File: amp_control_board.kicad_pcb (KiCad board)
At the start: 2 copper layers, 75 parts, among them J1 Conn_01x03_Male, J2 Conn_01x04_Female, J3 Screw_Terminal_01x03, J4 Screw_Terminal_01x02, J5 Conn_01x04_Female, J6 Conn_02x03_Odd_Even, J7 Conn_01x03_Male, M1 Fan_4pin, M2 Fan_4pin, Q1 BSP89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

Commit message: changing dev pc
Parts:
- moved SW3 78.4 mm to (113.4, 40.2)
- moved SW4 78.4 mm to (118.1, 40.2)
- moved U3 78.4 mm to (44.9, 74.5)
- moved C10 78.4 mm to (97.5, 77.7)
- moved C12 78.4 mm to (78.1, 82.5)
- moved C14 78.4 mm to (92.6, 71.8)
- moved C18 78.4 mm to (119.6, 55.4)
- moved C6 78.4 mm to (73.4, 82.5)
- moved C9 78.4 mm to (55.0, 80.1)
- moved D1 78.4 mm to (83.4, 64.9)
- moved D2 78.4 mm to (111.9, 52.4)
- moved J3 78.4 mm to (28.1, 66.0)
- moved J4 78.4 mm to (54.2, 74.0)
- moved J6 78.4 mm to (125.2, 35.7)
- moved J7 78.4 mm to (108.8, 58.1)
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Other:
- board outline added: 100.1 x 61 mm
- rule trace_min: 0.2 -> 0.1016
- rule via_min_drill: 0.3 -> 0.254
- rule via_min_size: 0.4 -> 0.254

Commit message: started floorplan
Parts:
- moved C9 146.2 mm to (173.0, -6.35), turned to 90 degrees
- moved DS1 146.1 mm to (282.6, 57.1)
- moved Y2 140.0 mm to (150.2, 158.7)
- moved D3 138.8 mm to (147.3, 182.2)
- moved C7 138.0 mm to (141.6, -20.3), turned to 90 degrees
- moved J1 136.3 mm to (172.7, 154.3), turned to 180 degrees
- moved J6 135.2 mm to (124.5, 170.8)
- moved U3 134.3 mm to (151.1, -7.62), turned to 270 degrees
- moved C5 134.0 mm to (134.6, -24.8), turned to 180 degrees
- moved R7 131.8 mm to (142.2, 182.2)
- moved R15 129.4 mm to (135.9, 173.4)
- moved C1 126.8 mm to (121.5, -24.8)
- moved Y1 125.7 mm to (146.1, 140.3)
- moved U1 125.6 mm to (151.8, -21.0)
- moved C8 125.6 mm to (157.5, 161.9)
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
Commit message: Adding changes 2008
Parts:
- J1, J3, M1, M2, SW2, SW3, SW4: moved to B.Cu
- moved M1 200.8 mm to (210.2, 74.3), turned to 180 degrees
- moved R23 188.7 mm to (214.6, 71.1)
- moved M2 185.9 mm to (175.3, 74.3), turned to 180 degrees
- moved SW4 185.9 mm to (215.3, 111.8)
- moved SW3 182.8 mm to (204.5, 111.8)
- moved SW2 179.3 mm to (193.7, 111.8)
- moved J3 173.3 mm to (133.3, 111.8), turned to 270 degrees
- moved R22 172.5 mm to (218.4, 71.1)
- moved R26 156.0 mm to (184.8, 71.8)
- moved R27 136.9 mm to (179.8, 71.8)
- moved R19 130.5 mm to (209.6, 110.5), turned to 90 degrees
- moved R18 128.6 mm to (209.6, 104.8), turned to 90 degrees
- moved R3 127.4 mm to (220.0, 75.6)
- moved R25 126.3 mm to (186.1, 76.2)
- moved R20 125.8 mm to (220.3, 104.8), turned to 90 degrees
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
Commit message: finished floorplan of top layer
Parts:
- C1: footprint Capacitor_SMD:C_0805_2012Metric_Pad1.18x1.45mm_HandSolder -> Capacitor_SMD:CP_Elec_10x12.5
- C13, C15, C16, C18: footprint Resistor_SMD:R_0805_2012Metric_Pad1.20x1.40mm_HandSolder -> Resistor_SMD:R_0402_1005Metric_Pad0.72x0.64mm_HandSolder
- C5, C7, C9: footprint Capacitor_SMD:C_0805_2012Metric_Pad1.18x1.45mm_HandSolder -> Capacitor_SMD:CP_Elec_10x10
- J3: value Screw_Terminal_01x03 -> Conn_01x03_Male; footprint TerminalBlock:TerminalBlock_bornier-3_P5.08mm -> Connector_PinHeader_2.54mm:PinHeader_1x03_P2.54mm_Vertical
- moved DS1 260.5 mm to (37.5, 145.4)
- moved C9 175.6 mm to (51.7, 120.7)
- moved U1 175.6 mm to (30.5, 106.0)
- moved U3 175.6 mm to (29.8, 119.4)
- moved C7 148.6 mm to (72.4, 111.1)
- moved C1 143.2 mm to (56.5, 102.9)
- moved U2 143.0 mm to (53.3, 90.8)
- moved C5 136.6 mm to (71.8, 96.5), turned to 270 degrees
- moved J4 135.1 mm to (28.6, 70.5)
- moved C11 101.2 mm to (185.4, 121.9)
- moved SW1 100.7 mm to (184.8, 116.8)
- moved R4 99.6 mm to (180.3, 121.9), turned to 180 degrees
- moved J7 97.8 mm to (28.6, 52.1)
- moved D3 89.2 mm to (140.3, 93.3)
- moved R7 89.1 mm to (135.9, 93.3)
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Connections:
- U5 pad 39: Net-(U5-Pad39) -> BTN_MODE
- U5 pad 40: Net-(U5-Pad40) -> BTN_UP
- U5 pad 41: Net-(U5-Pad41) -> BTN_DOWN

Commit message: completed preliminary floorplan for both top and bottom
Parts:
- C1, C5, C7, C9, J2, J4, J7, U1, U2, U3: moved to B.Cu
- moved U3 140.7 mm to (170.2, 108.6), turned to 0 degrees
- moved J2 132.4 mm to (155.6, 71.1), turned to 270 degrees
- moved U1 126.8 mm to (156.8, 95.2), turned to 180 degrees
- moved C9 122.9 mm to (172.1, 95.9)
- moved J7 115.9 mm to (132.7, 102.9)
- moved J4 105.4 mm to (134.0, 72.4)
- moved U2 92.8 mm to (146.1, 85.7), turned to 90 degrees
- moved C5 86.1 mm to (156.8, 83.2)
- moved C7 84.6 mm to (156.8, 106.7), turned to 180 degrees
- moved C1 82.4 mm to (136.5, 83.2), turned to 180 degrees
- moved DS1 12.1 mm to (29.2, 154.3)

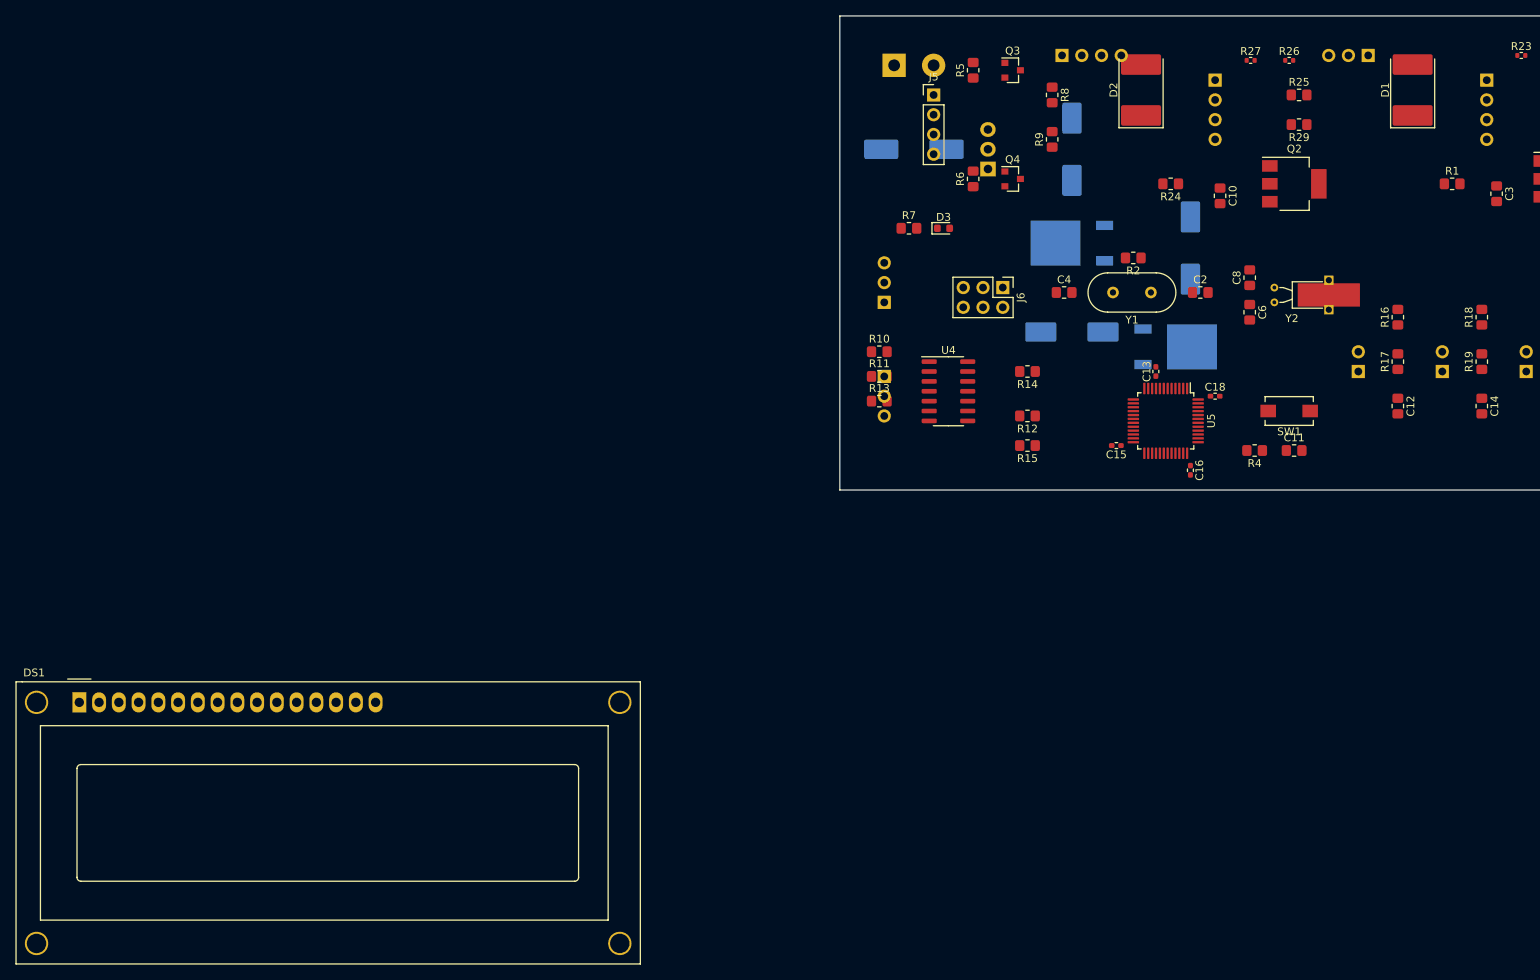
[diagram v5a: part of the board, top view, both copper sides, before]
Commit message: routeed power for bottom plane
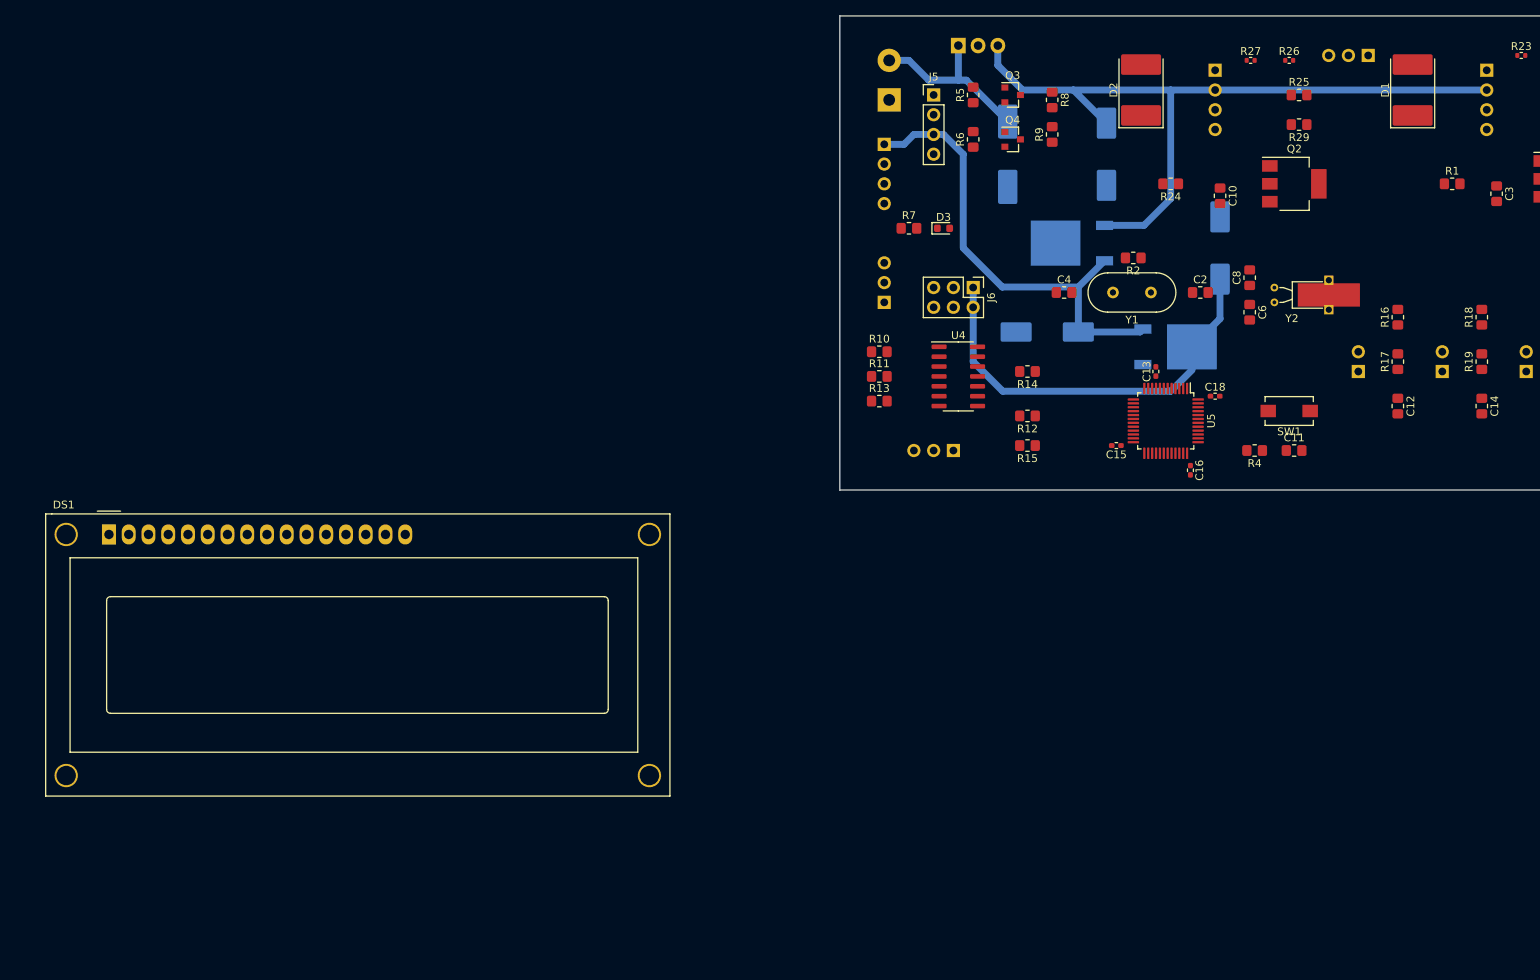
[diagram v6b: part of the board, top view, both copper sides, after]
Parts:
- moved J2 25.6 mm to (132.7, 82.5), turned to 180 degrees
- moved DS1 21.9 mm to (33.0, 132.7)
- moved U2 16.3 mm to (142.2, 69.8), turned to 0 degrees
- moved J3 13.0 mm to (141.6, 121.9), turned to 90 degrees
- moved C1 12.1 mm to (148.6, 83.8), turned to 270 degrees
- moved Q4 5.08 mm to (149.2, 81.9)
- moved R6 5.08 mm to (144.1, 81.9)
- moved J4 4.49 mm to (133.3, 76.8), turned to 90 degrees
- moved C5 4.49 mm to (161.3, 83.8)
- moved C9 3.81 mm to (175.9, 95.9)
- moved J6 3.81 mm to (144.1, 101.0)
- moved C7 3.18 mm to (153.7, 106.7)
- moved Q3 3.17 mm to (149.2, 76.2)
- moved R5 3.17 mm to (144.1, 76.2)
- moved U4 2.29 mm to (142.2, 112.4)
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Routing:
- net VDD_12V: track 0.00 -> 96.6 mm
- net VDD_5V: track 0.00 -> 59.7 mm
- net VDD_3V3: track 0.00 -> 53.5 mm
- net VIN_DC: track 0.00 -> 22.9 mm

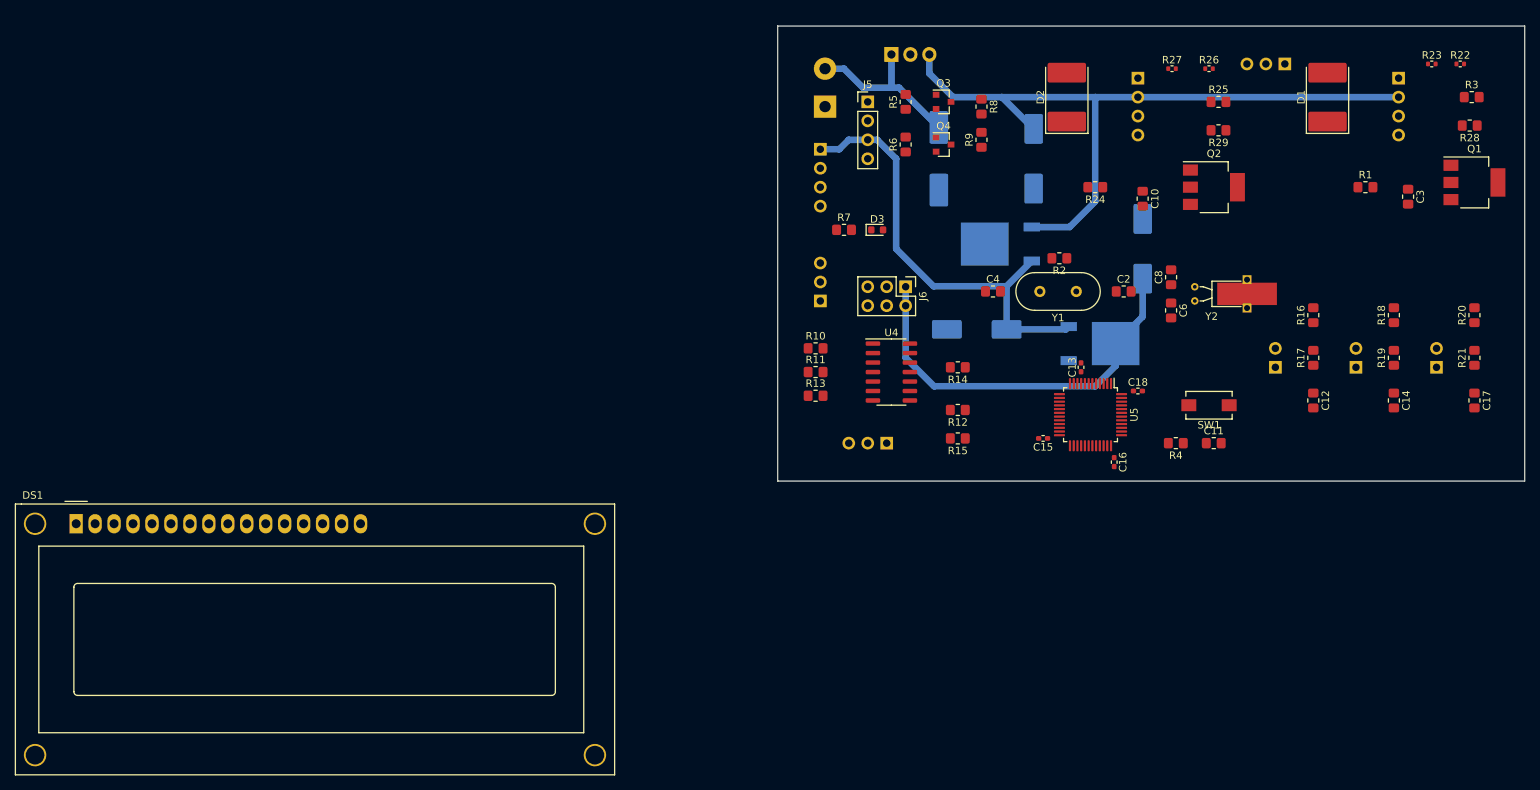
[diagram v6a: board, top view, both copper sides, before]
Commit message: top routing about 70% done
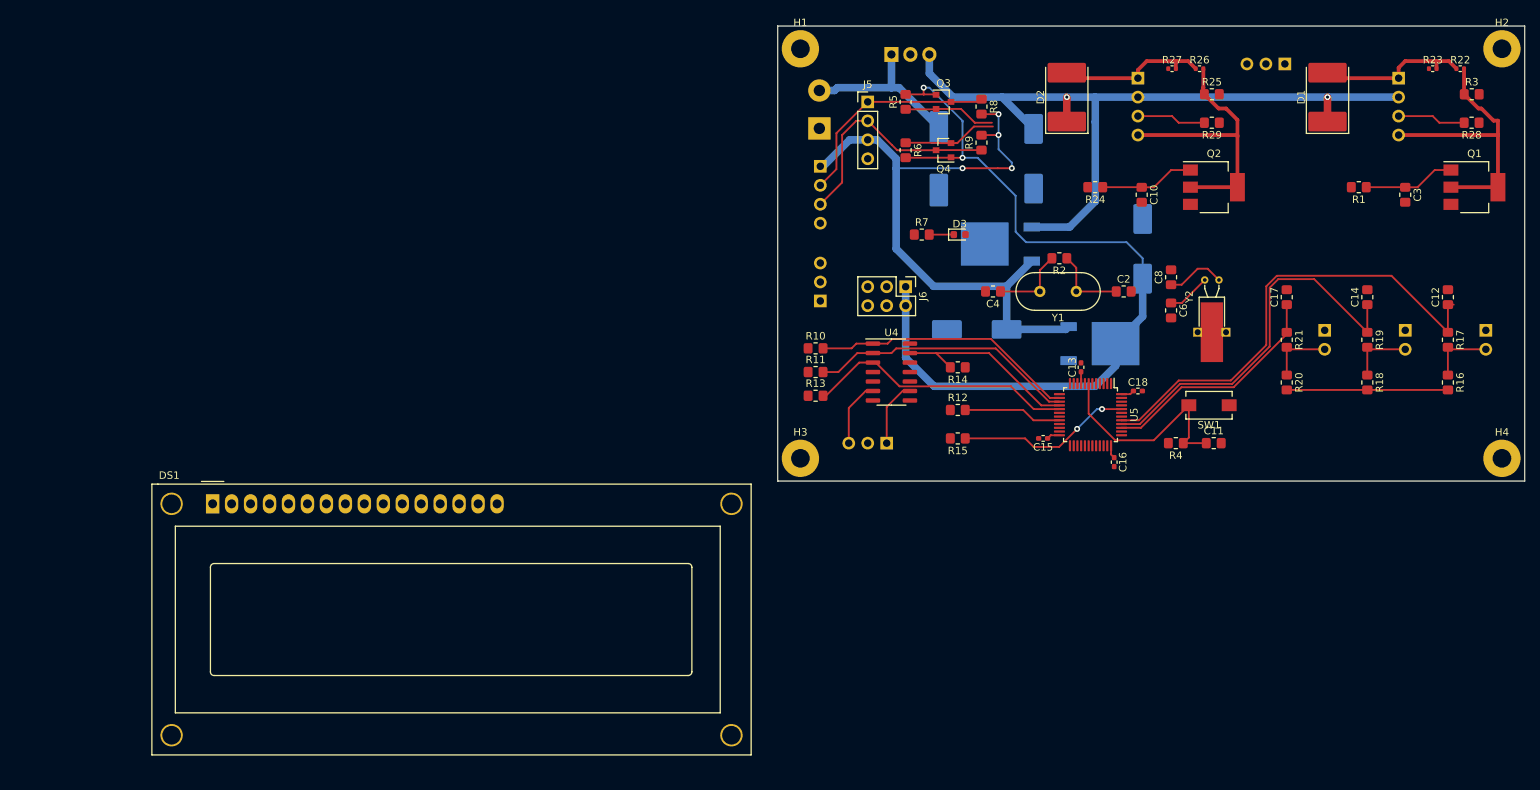
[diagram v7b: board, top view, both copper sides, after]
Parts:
- added H1: MountingHole, MountingHole:MountingHole_2.5mm_Pad, F.Cu at (130.0, 69.1)
- added H2: MountingHole, MountingHole:MountingHole_2.5mm_Pad, F.Cu at (224.0, 69.1)
- added H3: MountingHole, MountingHole:MountingHole_2.5mm_Pad, F.Cu at (130.0, 124.0)
- added H4: MountingHole, MountingHole:MountingHole_2.5mm_Pad, F.Cu at (224.0, 124.0)
- moved C17 28.7 mm to (195.2, 102.4), turned to 90 degrees
- moved SW2 28.6 mm to (221.9, 106.8), turned to 180 degrees
- moved R20 26.7 mm to (195.2, 113.8), turned to 270 degrees
- moved R21 25.3 mm to (195.2, 108.1), turned to 270 degrees
- moved C12 22.7 mm to (216.8, 102.4), turned to 90 degrees
- moved R16 20.2 mm to (216.8, 113.8), turned to 270 degrees
- moved DS1 18.5 mm to (51.3, 130.0)
- moved R17 18.2 mm to (216.8, 108.1), turned to 270 degrees
- moved SW4 15.8 mm to (200.3, 106.8), turned to 180 degrees
- moved C14 14.3 mm to (206.0, 102.4), turned to 90 degrees
- moved D3 11.1 mm to (151.4, 94.0)
- moved R7 10.4 mm to (146.3, 94.0)
- moved R18 9.69 mm to (206.0, 113.8), turned to 270 degrees
- moved SW3 8.26 mm to (211.1, 106.8), turned to 180 degrees
- moved R19 4.30 mm to (206.0, 108.1), turned to 270 degrees
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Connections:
- U5 pad 39: BTN_MODE -> BTN_DOWN
- U5 pad 41: BTN_DOWN -> BTN_MODE
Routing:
- net VDD_3V3: track 53.5 -> 142.0 mm, vias 0 -> 2
- net BTN_MODE: track 0.00 -> 64.0 mm
- net BTN_UP: track 0.00 -> 52.3 mm
- net Net-(M2-Pad4): track 0.00 -> 38.0 mm
- net Net-(M1-Pad4): track 0.00 -> 38.0 mm
- net SPI_MOSI: track 0.00 -> 36.1 mm
- net SPI_SCK: track 0.00 -> 35.9 mm
- net SPI_NSS: track 0.00 -> 35.5 mm
- net I2C_SDA_5V: track 0.00 -> 32.2 mm
- net BTN_DOWN: track 0.00 -> 31.3 mm
- net NRST: track 0.00 -> 29.3 mm
- net I2C_SCL_5V: track 0.00 -> 29.2 mm
- net VDD_5V: track 59.7 -> 88.7 mm, vias 0 -> 4
- net SPI_MISO: track 0.00 -> 25.6 mm
- net BOOT0: track 0.00 -> 23.5 mm, vias 0 -> 2
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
